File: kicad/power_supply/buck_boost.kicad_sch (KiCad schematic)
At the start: 3 parts, among them U401 TPS552872RYQR

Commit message: schematic capture
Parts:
- added C401, C421: 47u, symbol Device:C_Polarized_Small
- added C402, C403: 10u, symbol Device:C_Small
- added C404, C415: 1u, symbol Device:C_Small
- added C405, C409, C410, C411, C412, C413: 100n, symbol Device:C_Small
- added C407, C414: 10n, symbol Device:C_Small
- added C416: 100p, symbol Device:C_Small
- added C417, C418, C419, C420: 22u, symbol Device:C_Small
- added L401: 1u, symbol Device:L_Small
- added R401: 9.31k, symbol Device:R_Small_US
- added R402: 150k, symbol Device:R_Small_US
- added R403: 8.06k, symbol Device:R_Small_US
- added R404, R405: 10, symbol Device:R_Small_US
- added R406: 20m, symbol Device:R_Small_US
- added R407: 100k, symbol Device:R_Small_US
- C406: renamed from C402; value C_Small -> 100n
- C408: renamed from C401; value C_Small -> 4.7u
- U401: value TPS552872RYQR -> ~; MPN (none) -> TPS552872RYQR
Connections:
- net GND: now also U401.9 (PGND), C401.2, C402.2, C403.2, C404.2, C405.2, C407.2, C411.2, C413.2, C414.2, C415.2, C416.2, C417.2, C418.2, C419.2, C420.2, C421.2, R401.2, R402.2
- net VIN: now also C401.1, C402.1, C403.1, C404.1, C405.1
- net at U401.10 (SW2): now also C410.1, L401.2
- net at U401.11 (VOUT): now also C411.1, C413.1, C415.1, C417.1, C418.1, C419.1, C420.1, C421.1, R404.1, R406.1
- net at U401.12 (ISP): now also C412.1, R404.2
- net at U401.13 (ISN): now also C412.2, R405.2
- net FB_BT: now reaches U401.14 (FB)
- net FB_BT: now also R407.1
- net at U401.15 (COMP): now also C416.1, R403.1
- net at U401.16 (CDC): now also R402.1
- net VCC: now reaches C408.1, U401.18 (VCC)
- net VCC: now also U401.2 (MODE)
- net at U401.19 (BOOT2): now also C410.2
- net at U401.20 (BOOT1): now also C409.2
- net PG: now reaches U401.3 (PG)
- net at U401.5 (DITH/SYNC): now also C407.1
- net at U401.6 (FSW): now also R401.1
- net at U401.8 (SW1): now also C409.1, L401.1
- net EN/UVLO renamed EN
- new net: C414.1, R403.2
- new net VOUT: R405.1, R406.2, R407.2
- no-connect marks 1 -> 2
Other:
- note added: "1.2*100k R_{FB_BT} = --------- V_{OUT} - 1.2"
- note added: "Note: To set output voltage, V_{OUT}, connect 'FB_BT' through R_{FB_BT} to ground to set output voltage."
- note added: "V_{REF}*R_{FB_UP} R_{FB_BT} = --------- V_{OUT} - V_{REF}"
- note added: "ex. V_{OUT} = 12V, R_{FB_BT} = 11.1k"
- moved on the sheet: C406, C408

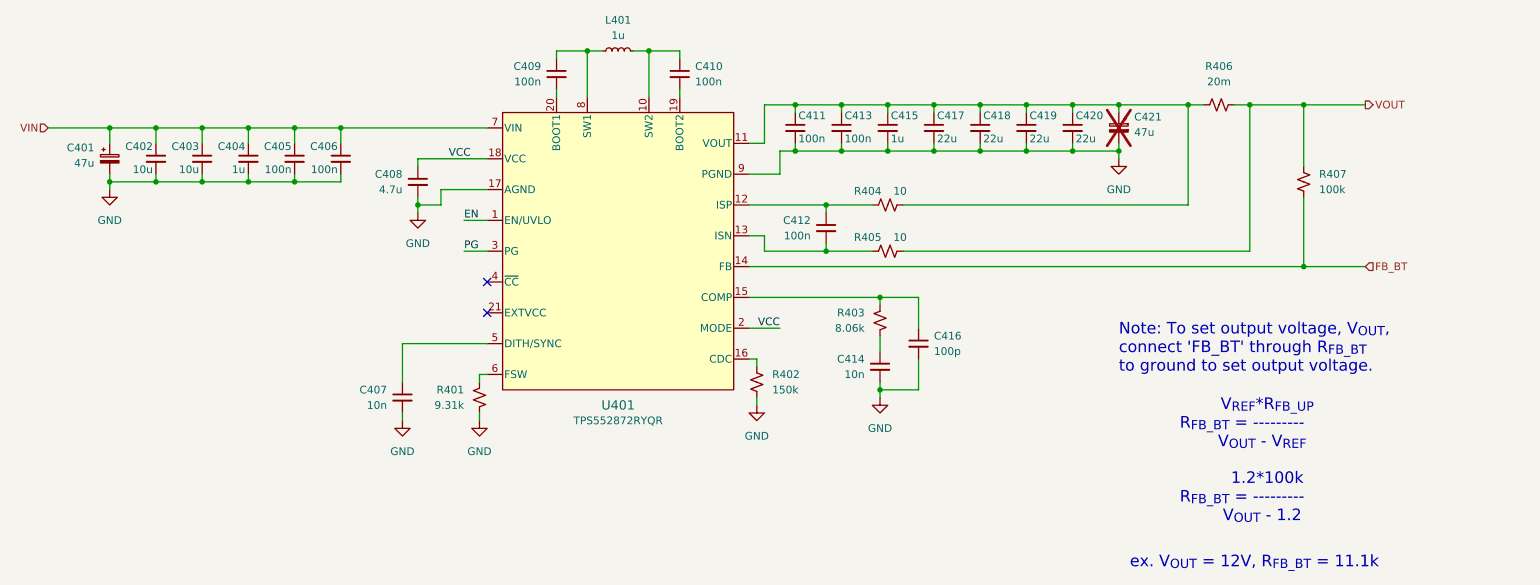
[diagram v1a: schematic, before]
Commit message: improved load switch mosfet paste aperture
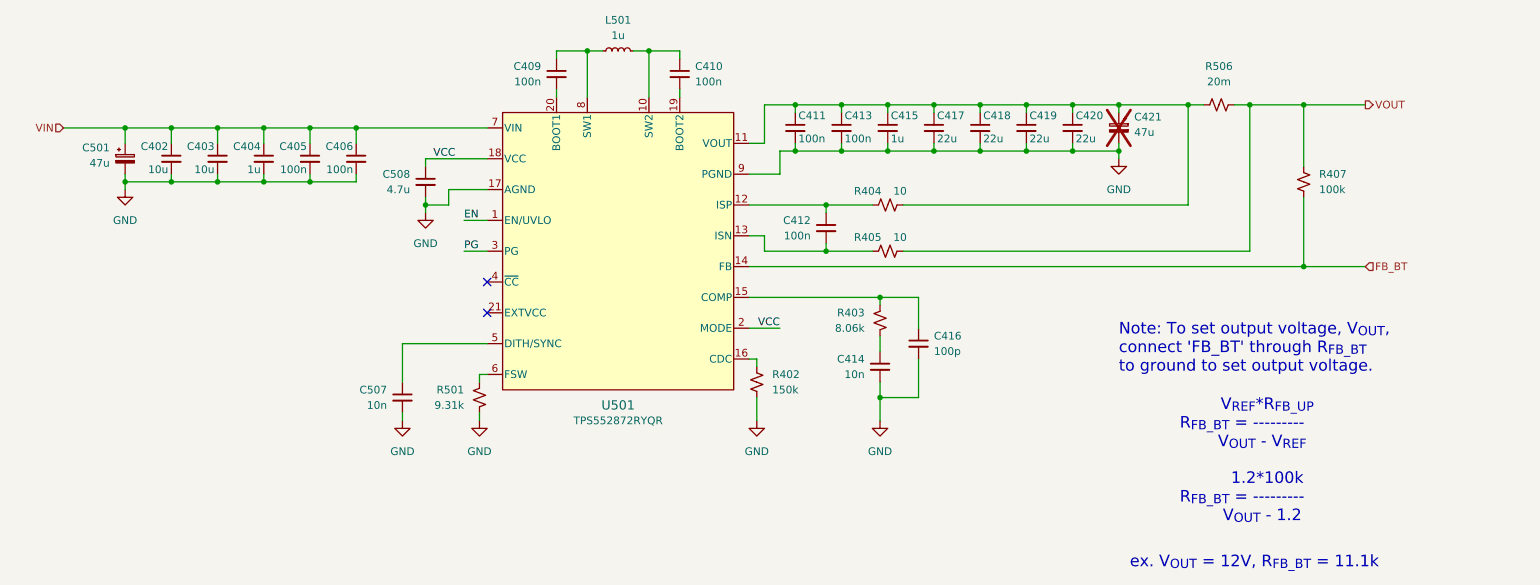
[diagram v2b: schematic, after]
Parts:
- renumbered C401 to C501, C407 to C507, C408 to C508, L401 to L501, R401 to R501, R406 to R506, U401 to U501
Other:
- moved on the sheet: C402, C403, C404, C405, C406, C501, C508

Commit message: schematic capture
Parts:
- renumbered C501 to C601, C402 to C602, C403 to C603, C404 to C604, C405 to C605, C406 to C606, C507 to C607, C508 to C608, C409 to C609, C410 to C610, C411 to C611, C412 to C612, C413 to C613, C414 to C614, C415 to C615, C416 to C616, C417 to C617, C418 to C618, C419 to C619, C420 to C620, C421 to C621, L501 to L601, R501 to R601, R402 to R602, R403 to R603, R404 to R604, R405 to R605, R506 to R606, R407 to R607, U501 to U601
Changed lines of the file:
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@@
 		(on_board yes)
 		(dnp no)
-		(property "Reference" "R402"
+		(property "Reference" "R602"
 			(at 161.29 116.8399 0)
 			(effects
@@
 		(on_board yes)
 		(dnp no)
-		(property "Reference" "C419"
+		(property "Reference" "C619"
 			(at 203.708 74.168 0)
 			(effects
@@
 		(dnp no)
 		(fields_autoplaced yes)
-		(property "Reference" "#PWR0407"
+		(property "Reference" "#PWR0607"
 			(at 218.44 87.63 0)
 			(effects
@@
 		(on_board yes)
 		(dnp no)
-		(property "Reference" "C413"
+		(property "Reference" "C613"
 			(at 173.228 74.168 0)
 			(effects
@@
 		(dnp no)
 		(fields_autoplaced yes)
-		(property "Reference" "#PWR0406"
+		(property "Reference" "#PWR0606"
 			(at 179.07 130.81 0)
 			(effects
@@
 		(on_board yes)
 		(dnp no)
-		(property "Reference" "C406"
+		(property "Reference" "C606"
 			(at 92.202 79.248 0)
 			(effects
@@
 		(on_board yes)
 		(dnp no)
-		(property "Reference" "C420"
+		(property "Reference" "C620"
 			(at 211.328 74.168 0)
 			(effects
@@
 		(dnp no)
 		(fields_autoplaced yes)
-		(property "Reference" "#PWR0401"
+		(property "Reference" "#PWR0601"
 			(at 54.61 92.71 0)
 			(effects
@@
 		(on_board yes)
 		(dnp no)
-		(property "Reference" "R405"
+		(property "Reference" "R605"
 			(at 177.038 94.234 90)
 			(effects
@@
 		(on_board yes)
 		(dnp no)
-		(property "Reference" "C417"
+		(property "Reference" "C617"
 			(at 188.468 74.168 0)
 			(effects
@@
 		(on_board yes)
 		(dnp no)
-		(property "Reference" "C414"
+		(property "Reference" "C614"
 			(at 176.53 114.3062 0)
 			(effects
@@
 		(on_board yes)
 		(dnp no)
-		(property "Reference" "C508"
+		(property "Reference" "C608"
 			(at 101.6 83.8262 0)
 			(effects
@@
 					(unit 1)
 				)
+				(path "/6a7d9dc9-f78f-470f-911b-b95256023173/cf53f1a5-f32c-4d02-84d0-a76cca0772c3"
+					(reference "C408")
+					(unit 1)
+				)
 				(path "/6a7d9dc9-f78f-470f-911b-b95256023173/d1fcefd7-3ecc-4716-9879-f129c42734ff"
 					(reference "C508")
@@
 		(on_board yes)
 		(dnp no)
-		(property "Reference" "C501"
+		(property "Reference" "C601"
 			(at 52.07 79.4638 0)
 			(effects
@@
 					(unit 1)
 				)
+				(path "/6a7d9dc9-f78f-470f-911b-b95256023173/cf53f1a5-f32c-4d02-84d0-a76cca0772c3"
+					(reference "C401")
+					(unit 1)
+				)
 				(path "/6a7d9dc9-f78f-470f-911b-b95256023173/d1fcefd7-3ecc-4716-9879-f129c42734ff"
 					(reference "C501")
@@
 		(on_board yes)
 		(dnp no)
-		(property "Reference" "C416"
+		(property "Reference" "C616"
 			(at 187.96 110.4962 0)
 			(effects
@@
 		(on_board yes)
 		(dnp no)
-		(property "Reference" "C402"
+		(property "Reference" "C602"
 			(at 61.722 79.248 0)
 			(effects
@@
 		(on_board yes)
 		(dnp no)
-		(property "Reference" "C410"
+		(property "Reference" "C610"
 			(at 148.59 66.0462 0)
 			(effects
@@
 		(on_board yes)
 		(dnp no)
-		(property "Reference" "C405"
+		(property "Reference" "C605"
 			(at 84.582 79.248 0)
 			(effects
@@
 		(dnp no)
 		(fields_autoplaced yes)
-		(property "Reference" "#PWR0404"
+		(property "Reference" "#PWR0604"
 			(at 113.03 130.81 0)
 			(effects
@@
 		(on_board yes)
 		(dnp no)
-		(property "Reference" "C507"
+		(property "Reference" "C607"
 			(at 97.79 119.3862 0)
 			(effects
@@
 				(path "/6a7d9dc9-f78f-470f-911b-b95256023173/c2fcbfb1-6741-44cb-a82c-7741918cd8a1"
 					(reference "C607")
+					(unit 1)
+				)
+				(path "/6a7d9dc9-f78f-470f-911b-b95256023173/cf53f1a5-f32c-4d02-84d0-a76cca0772c3"
+					(reference "C407")
 					(unit 1)
 				)
@@
 		(on_board yes)
 		(dnp no)
-		(property "Reference" "C404"
+		(property "Reference" "C604"
 			(at 76.962 79.248 0)
 			(effects
@@
 		(dnp no)
 		(fields_autoplaced yes)
-		(property "Reference" "L501"
+		(property "Reference" "L601"
 			(at 135.89 58.42 90)
 			(effects
@@
 				(path "/6a7d9dc9-f78f-470f-911b-b95256023173/c2fcbfb1-6741-44cb-a82c-7741918cd8a1"
 					(reference "L601")
+					(unit 1)
+				)
+				(path "/6a7d9dc9-f78f-470f-911b-b95256023173/cf53f1a5-f32c-4d02-84d0-a76cca0772c3"
+					(reference "L401")
 					(unit 1)
 				)
@@
 		(on_board yes)
 		(dnp no)
-		(property "Reference" "C403"
+		(property "Reference" "C603"
 			(at 69.342 79.248 0)
 			(effects
@@
 		(on_board yes)
 		(dnp no)
-		(property "Reference" "C409"
+		(property "Reference" "C609"
 			(at 123.19 66.0462 0)
 			(effects
@@
 		(on_board yes)
 		(dnp no)
-		(property "Reference" "C411"
+		(property "Reference" "C611"
 			(at 165.608 74.168 0)
 			(effects
@@
 		(dnp no)
 		(fields_autoplaced yes)
-		(property "Reference" "#PWR0403"
+		(property "Reference" "#PWR0603"
 			(at 104.14 96.52 0)
 			(effects
@@
 		(on_board yes)
 		(dnp yes)
-		(property "Reference" "C421"
+		(property "Reference" "C621"
 			(at 220.98 74.3838 0)
 			(effects
@@
 		(dnp no)
 		(fields_autoplaced yes)
-		(property "Reference" "#PWR0402"
+		(property "Reference" "#PWR0602"
 			(at 100.33 130.81 0)
 			(effects
@@
 		(on_board yes)
 		(dnp no)
-		(property "Reference" "C412"
+		(property "Reference" "C612"
 			(at 167.64 91.4462 0)
 			(effects
@@
 		(dnp no)
 		(fields_autoplaced yes)
-		(property "Reference" "#PWR0405"
+		(property "Reference" "#PWR0605"
 			(at 158.75 130.81 0)
 			(effects
@@
 		(on_board yes)
 		(dnp no)
-		(property "Reference" "R404"
+		(property "Reference" "R604"
 			(at 177.038 86.614 90)
 			(effects
@@
 		(on_board yes)
 		(dnp no)
-		(property "Reference" "C415"
+		(property "Reference" "C615"
 			(at 180.848 74.168 0)
 			(effects
@@
 		(on_board yes)
 		(dnp no)
-		(property "Reference" "R501"
+		(property "Reference" "R601"
 			(at 110.49 119.3799 0)
 			(effects
@@
 					(unit 1)
 				)
+				(path "/6a7d9dc9-f78f-470f-911b-b95256023173/cf53f1a5-f32c-4d02-84d0-a76cca0772c3"
+					(reference "R401")
+					(unit 1)
+				)
 				(path "/6a7d9dc9-f78f-470f-911b-b95256023173/d1fcefd7-3ecc-4716-9879-f129c42734ff"
 					(reference "R501")
@@
 		(dnp no)
 		(fields_autoplaced yes)
-		(property "Reference" "U501"
+		(property "Reference" "U601"
 			(at 135.89 121.92 0)
 			(effects
@@
 				(path "/6a7d9dc9-f78f-470f-911b-b95256023173/c2fcbfb1-6741-44cb-a82c-7741918cd8a1"
 					(reference "U601")
+					(unit 1)
+				)
+				(path "/6a7d9dc9-f78f-470f-911b-b95256023173/cf53f1a5-f32c-4d02-84d0-a76cca0772c3"
+					(reference "U401")
 					(unit 1)
 				)
@@
 		(on_board yes)
 		(dnp no)
-		(property "Reference" "R403"
+		(property "Reference" "R603"
 			(at 176.53 106.6799 0)
 			(effects
@@
 		(dnp no)
 		(fields_autoplaced yes)
-		(property "Reference" "R506"
+		(property "Reference" "R606"
 			(at 234.95 66.04 90)
 			(effects
@@
 					(unit 1)
 				)
+				(path "/6a7d9dc9-f78f-470f-911b-b95256023173/cf53f1a5-f32c-4d02-84d0-a76cca0772c3"
+					(reference "R406")
+					(unit 1)
+				)
 				(path "/6a7d9dc9-f78f-470f-911b-b95256023173/d1fcefd7-3ecc-4716-9879-f129c42734ff"
 					(reference "R506")
@@
 		(dnp no)
 		(fields_autoplaced yes)
-		(property "Reference" "R407"
+		(property "Reference" "R607"
 			(at 251.46 83.8199 0)
 			(effects
@@
 		(on_board yes)
 		(dnp no)
-		(property "Reference" "C418"
+		(property "Reference" "C618"
 			(at 196.088 74.168 0)
 			(effects
